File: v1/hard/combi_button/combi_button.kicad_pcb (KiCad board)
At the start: 2 copper layers, 82 x 44 mm, 44 parts, among them J1 RJ12, J10 Conn_01x02_Female, J11 Conn_02x02_Odd_Even, J12 Conn_02x02_Odd_Even, J2 RJ12, J3 RJ12, J4 RJ12, J5 Barrel_Jack_Switch, J6 Conn_01x04_Female, J7 Conn_01x04_Female, J8 Barrel_Jack_Switch, J9 Conn_01x02_Female, Q1 Q_PMOS_GSD, Q2 Q_PMOS_GSD, U1 LM393, U2 LM393, U3 PC817, U4 PC817, U5 PC817

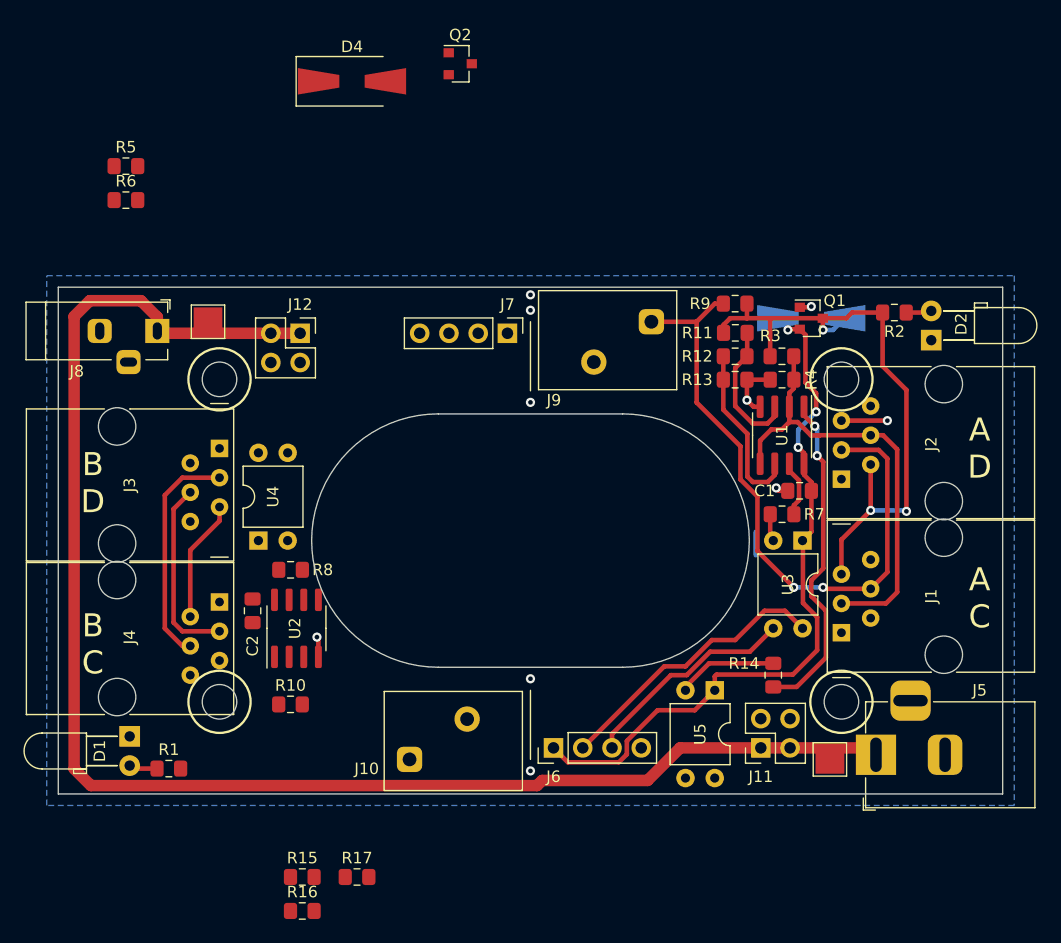
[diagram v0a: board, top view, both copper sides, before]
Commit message: Moved connectors location to 2.54 grid for better compartibility with predrilled prototyping boards.
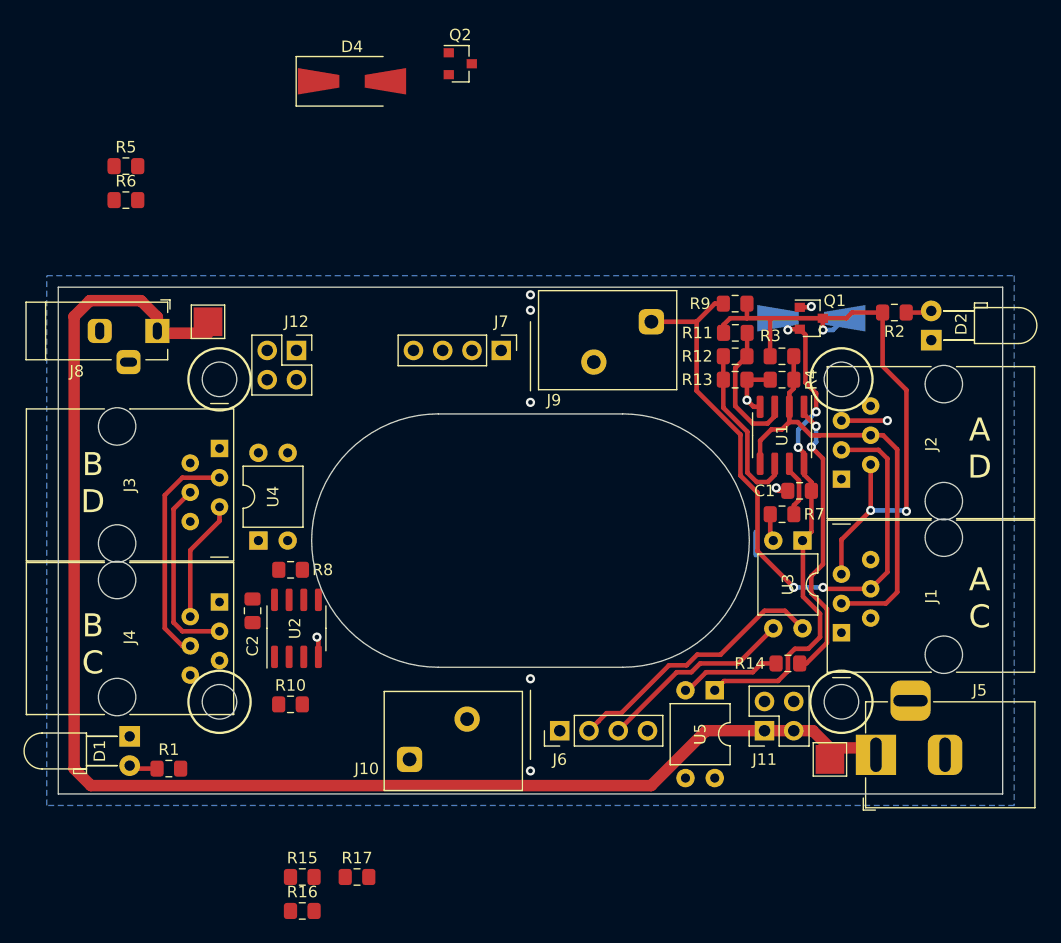
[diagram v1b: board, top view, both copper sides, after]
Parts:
- moved R14 1.63 mm to (122.4, 110.7), turned to 0 degrees
- moved J6 1.58 mm to (102.5, 116.5)
- moved J7 1.58 mm to (97.5, 83.5)
- moved J11 1.52 mm to (120.3, 116.5)
- moved J12 1.52 mm to (79.7, 83.5)
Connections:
- J6 pad 2: Net-(J6-Pad2) -> /OPT_C
- J6 pad 3: Net-(J6-Pad3) -> /OPT_E
- J7 pad 2: Net-(J7-Pad2) -> /OPT_C
- J7 pad 3: Net-(J7-Pad3) -> /OPT_E
- U3 pad 3: Net-(J6-Pad3) -> /OPT_E
- U3 pad 4: Net-(J6-Pad2) -> /OPT_C
- U4 pad 3: Net-(J7-Pad3) -> /OPT_E
- U4 pad 4: Net-(J7-Pad2) -> /OPT_C
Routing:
- net Net-(J6-Pad2): track 24.6 -> 0.00 mm
- net /OPT_C: track 0.00 -> 23.5 mm
- net Net-(J6-Pad3): track 19.0 -> 0.00 mm
- net VCC: track 61.7 -> 43.7 mm
- net /OPT_E: track 0.00 -> 17.1 mm
- net VDC: track 135.2 -> 128.4 mm
- net Net-(R14-Pad2): track 29.1 -> 25.6 mm

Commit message: Finished tracing of combi button PCB. V0.1 Prepared for manufactoring.
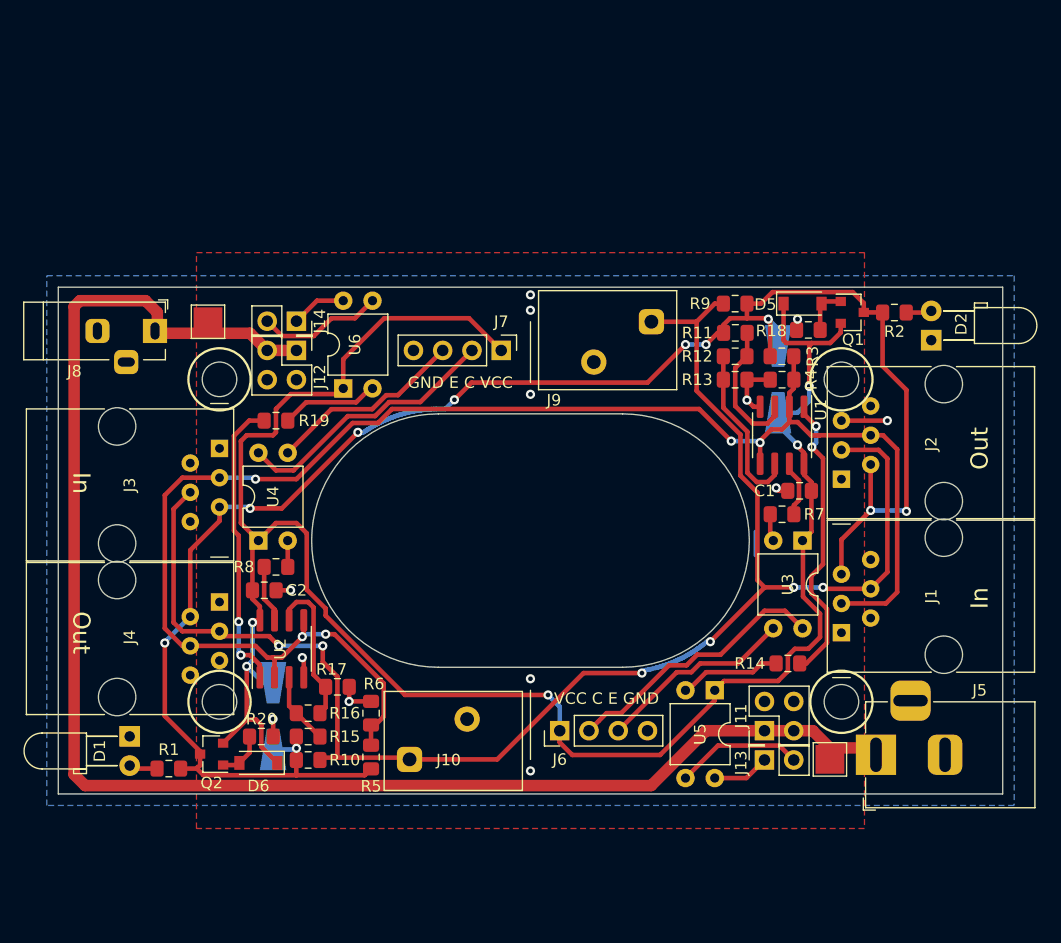
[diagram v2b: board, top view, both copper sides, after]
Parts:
- added D5: D_Zener, Diode_SMD:D_SOD-123, F.Cu at (123.6, 79.4)
- added D6: D_Zener, Diode_SMD:D_SOD-123, F.Cu at (76.4, 119.3)
- added J13: Conn_01x02_Male, Connector_PinSocket_2.54mm:PinSocket_1x02_P2.54mm_Vertical, F.Cu at (120.3, 119.0)
- added J14: Conn_01x02_Male, Connector_PinSocket_2.54mm:PinSocket_1x02_P2.54mm_Vertical, F.Cu at (79.7, 81.0)
- added R18: 1k, Resistor_SMD:R_0805_2012Metric_Pad1.15x1.40mm_HandSolder, F.Cu at (124.1, 81.7)
- added R19: 1k, Resistor_SMD:R_0805_2012Metric_Pad1.15x1.40mm_HandSolder, F.Cu at (77.9, 89.6)
- added R20: 1k, Resistor_SMD:R_0805_2012Metric_Pad1.15x1.40mm_HandSolder, F.Cu at (76.6, 117.0)
- added REF**: OSHW-Symbol_6.7x6mm_SilkScreen, Symbol:OSHW-Symbol_6.7x6mm_SilkScreen, B.Cu at (115.0, 86.5)
- added U6: PC817, Package_DIP:DIP-4_W7.62mm, F.Cu at (83.7, 86.8)
- D4: moved to B.Cu
- moved Q2 63.7 mm to (72.3, 118.5), turned to 180 degrees
- moved R5 55.5 mm to (86.2, 118.8), turned to 90 degrees
- moved D4 55.5 mm to (77.6, 115.2), turned to 270 degrees
- moved R6 49.4 mm to (86.2, 115.0), turned to 90 degrees
- moved R16 17.2 mm to (80.7, 115.0)
- moved R17 16.6 mm to (83.2, 112.7)
- moved R15 12.2 mm to (80.7, 117.0)
- moved D3 6.04 mm to (121.5, 86.0), turned to 90 degrees
- moved R10 5.06 mm to (80.7, 119.0)
- moved Q1 3.59 mm to (127.9, 80.2)
- moved U2 2.18 mm to (78.4, 109.4)
- moved C2 2.05 mm to (76.9, 104.3), turned to 0 degrees
- moved R8 1.30 mm to (77.9, 102.3), turned to 180 degrees
- moved J8 0.20 mm to (67.4, 81.8)
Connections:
- J7 pad 2: /OPT_C -> /OPT_C2
- J7 pad 3: /OPT_E -> /OPT_E2
- Q1 pad 1: GND -> Net-(D5-Pad2)
- Q2 pad 1: GND -> Net-(D6-Pad2)
- U2 pad 1: Net-(R8-Pad2) -> Net-(R19-Pad2)
- U2 pad 7: Net-(U2-Pad7) -> Net-(R8-Pad2)
- U4 pad 3: /OPT_E -> /OPT_E2
- U4 pad 4: /OPT_C -> /OPT_C2
- U5 pad 3: Net-(U5-Pad3) -> /E2_1
- U5 pad 4: Net-(U5-Pad4) -> /C2_1
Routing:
- net VCC: track 43.7 -> 175.6 mm, vias 3 -> 5
- net +5V: track 65.3 -> 155.3 mm, vias 3 -> 10
- net /MiddlePoint: track 58.9 -> 138.7 mm, vias 0 -> 5
- net /ButtonPoint: track 72.6 -> 138.4 mm, vias 2 -> 6
- net Net-(R19-Pad2): track 0.00 -> 25.5 mm, vias 0 -> 2
- net /OPT_C2: track 0.00 -> 23.5 mm
- net /OPT_E2: track 0.00 -> 17.1 mm
- net Net-(R16-Pad2): track 0.00 -> 13.4 mm
- net /E2_1: track 0.00 -> 11.1 mm
- net /E2_2: track 0.00 -> 10.9 mm
- net VDC: track 128.4 -> 137.9 mm
- net Net-(R19-Pad1): track 0.00 -> 8.51 mm
- net Net-(R15-Pad2): track 0.00 -> 6.26 mm
- net GND: track 15.1 -> 21.0 mm, vias 10 -> 13
- net Net-(R8-Pad2): track 0.00 -> 5.01 mm
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- added copper zone on F.Cu, net VCC
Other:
- board text added: "C"
- board text added: "E"
- board text added: "GND E C VCC"
- board text added: "In"
- board text added: "Out"
- board text added: "VCC C E GND"
- board text added: "combi button v 0.1 by DiMomite"
- board text removed: "A C"
- board text removed: "A D"
- board text removed: "B C"
- board text removed: "B D"
- board text removed: "Button only R9=4k7 R3,R4=10k"
- board text removed: "Reverse: Q1 OR D3 Not used: R14,J5"
